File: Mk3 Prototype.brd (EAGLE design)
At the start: 113 x 55.2 mm, 193 parts, among them IC1 BD49XXX, IC2 NCP1529MU, IC3 STM32F401V, IC4 CC3100, IC5 S25FL216K0PMFI011, J1 ZX62-AB-5PA(11), J2 SFV30R-2STE1HLF, J3 SWD_SHROUD, Q1 DMMT5401, Q2 NTR4101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

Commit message: first prototype pretty much done
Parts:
- added ANT2: CHIPANT, TiLDA Mk3 Parts:2450AT42A100
- JP4: value M10SILK_FEMALE_PTH -> M10NOSILK; device SparkFun-Connectors:1X10 -> TiLDA Mk3 Parts:1X10-NOSILK
- SV1: device con-lstb:MA03-1 -> TiLDA Mk3 Parts:1X03
- moved LOGO1 28.3 mm to (75.4, 22.1), turned to 0 degrees
- moved C70 10.4 mm to (82.5, 53.0), turned to 180 degrees
- moved ANT1 4.92 mm to (75.0, 58.5), turned to 0 degrees
- moved C67 3.93 mm to (82.5, 50.0), turned to 180 degrees
- moved X6 3.08 mm to (86.0, 51.0)
- moved FID4 3.00 mm to (2.50, 3.00)
- moved L7 3.00 mm to (82.0, 51.6)
- moved R41 3.00 mm to (82.5, 51.0)
- moved SV1 2.50 mm to (90.5, 47.0)
- moved FID1 0.67 mm to (2.90, 46.3)
- moved FID6 0.67 mm to (2.90, 46.3)
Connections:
- net ANT: now also ANT2.P$1; no longer ANT1.FEED
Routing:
- net ANT: track 13.2 -> 3.27 mm
- net N$2: track 3.17 -> 6.17 mm
- net N$18: track 98.1 -> 97.3 mm
- net N$48: track 0.72 -> 1.42 mm
- net I2C_SCL: track 52.5 -> 53.1 mm
- net GND: track 210.9 -> 210.8 mm, vias 162 -> 154
- added copper zone on layer 1, net N$29
- added copper zone on layer 16, net N$29
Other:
- board text added: "*"
- board text added: "M. Brejza, LWK, parag0n"

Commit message: minor touchups
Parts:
- moved C67 0.50 mm to (83.0, 50.0)
- moved C70 0.50 mm to (83.0, 53.0)
- moved L7 0.50 mm to (82.5, 51.6)
- moved R41 0.50 mm to (83.0, 51.0)
- moved SV1 0.20 mm to (90.5, 46.8)
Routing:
- net GND: track 210.8 -> 216.6 mm, vias 154 -> 157
- net +3V3: track 516.0 -> 512.0 mm
- net N$19: track 8.06 -> 5.13 mm
- net ANT: track 3.27 -> 4.62 mm
- net N$17: track 31.8 -> 30.8 mm
- net CC_FLASH_CLK: track 18.4 -> 17.6 mm
- net N$48: track 1.42 -> 0.92 mm
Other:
- outline, holes or cut-outs redrawn

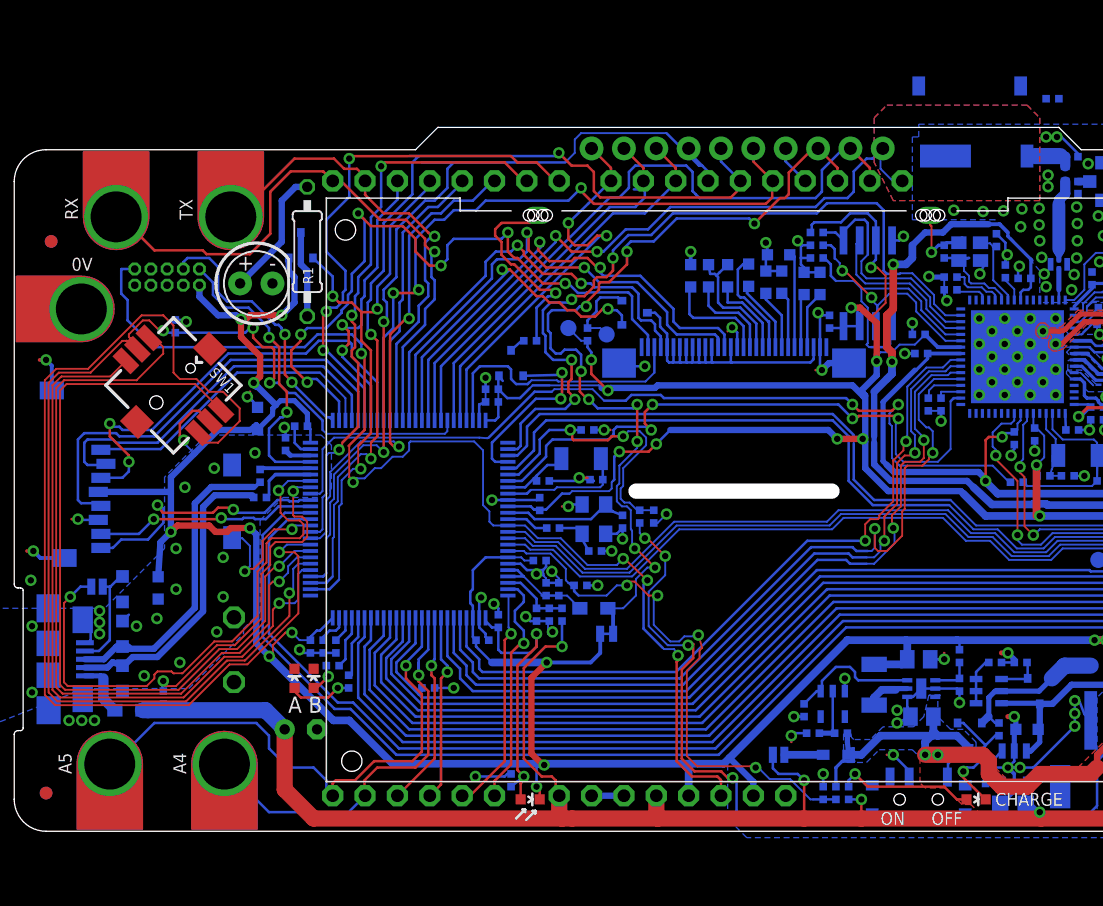
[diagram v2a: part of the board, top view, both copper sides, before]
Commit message: schematic tidyied up
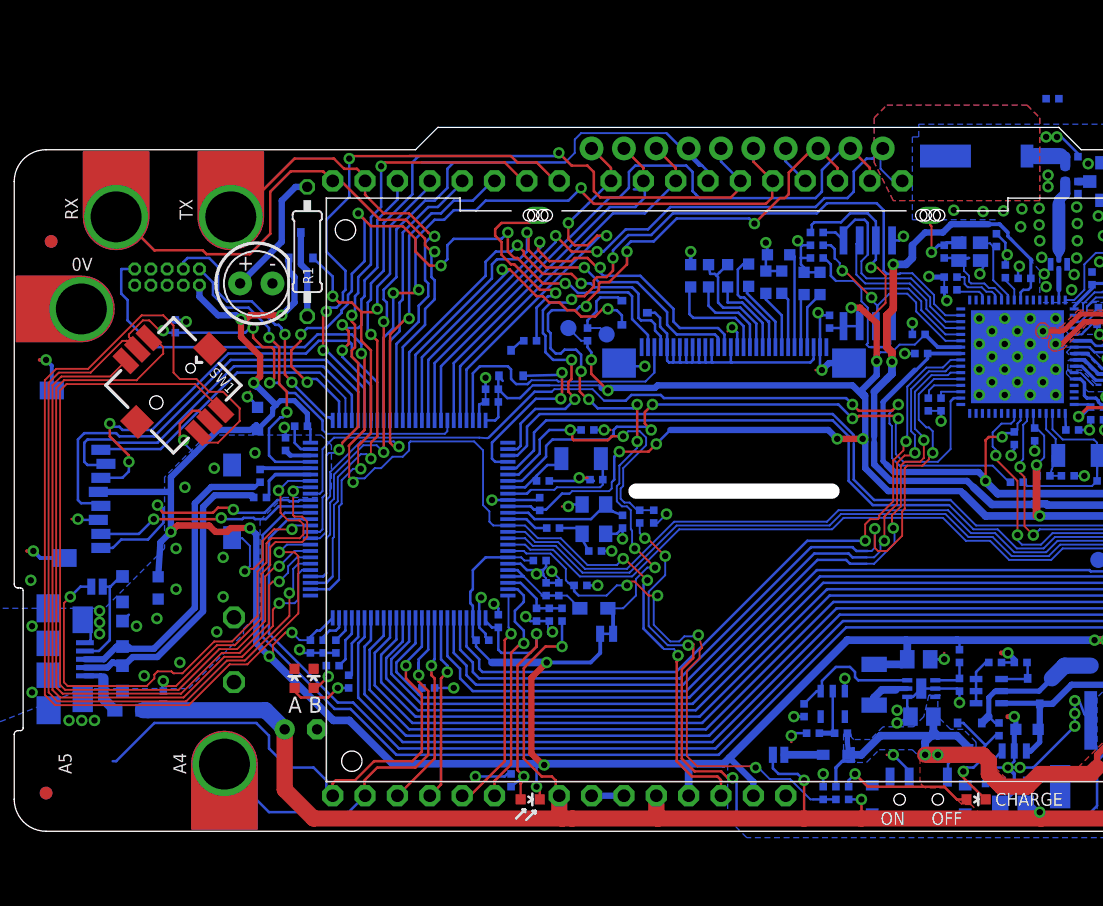
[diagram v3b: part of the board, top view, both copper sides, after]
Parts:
- removed ANT1: ANTENNA22500AT44M0400, SparkFun-RF:ANTENNA-CHIP_2500AT44M0400
- removed TP7: TP4MM, TiLDA Mk3 Parts:4MMEDGE
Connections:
- net A5: no longer TP7.P$1
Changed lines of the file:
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@@
 <?xml version="1.0" encoding="utf-8"?>
 <!DOCTYPE eagle SYSTEM "eagle.dtd">
-<eagle version="6.6.0">
+<eagle version="7.1.0">
 <drawing>
 <settings>
@@
 <pass name="Default">
 <param name="RoutingGrid" value="50mil"/>
+<param name="AutoGrid" value="1"/>
+<param name="Efforts" value="0"/>
+<param name="TopRouterVariant" value="1"/>
 <param name="tpViaShape" value="round"/>
 <param name="PrefDir.1" value="|"/>
@@
 <element name="TP8" library="TiLDA Mk3 Parts" package="4MMEDGE" value="TP4MM" x="16.5" y="4" smashed="yes" rot="R180"/>
 <element name="TP5" library="TiLDA Mk3 Parts" package="4MMEDGE" value="TP4MM" x="4" y="41" smashed="yes" rot="R90"/>
-<element name="TP7" library="TiLDA Mk3 Parts" package="4MMEDGE" value="TP4MM" x="7.5" y="4" smashed="yes" rot="R180"/>
 <element name="R18" library="TiLDA Mk3 Parts" package="R0402-SMALLER" value="0402/220k/5%" x="43" y="17" smashed="yes" rot="MR90">
 <attribute name="NAME" x="43.6015" y="15.889" size="0.8128" layer="26" font="vector" ratio="14" rot="MR270"/>
@@
 <attribute name="NAME" x="84.889" y="55.6985" size="0.8128" layer="26" font="vector" ratio="14" rot="MR0"/>
 </element>
-<element name="ANT1" library="SparkFun-RF" package="ANTENNA-CHIP_2500AT44M0400" value="ANTENNA22500AT44M0400" x="75" y="58.5" smashed="yes" rot="MR0"/>
 <element name="C8" library="TiLDA Mk3 Parts" package="C0402-SMALLER" value="0402/4u7/6.3V/X5R" x="37.5" y="34.7" smashed="yes" rot="MR180">
 <attribute name="NAME" x="36.389" y="34.5985" size="0.8128" layer="26" font="vector" ratio="14" rot="MR0"/>
@@
 <wire x1="30.75" y1="13.25" x2="32" y2="14.5" width="0.2" layer="16"/>
 <wire x1="32" y1="16.75" x2="32" y2="14.5" width="0.2" layer="16"/>
-<contactref element="TP7" pad="P$1"/>
 <wire x1="11" y1="8.5" x2="19" y2="8.5" width="0.2" layer="16"/>
 <wire x1="19" y1="8.5" x2="20" y2="7.5" width="0.2" layer="16"/>
@@
 <wire x1="11" y1="8.5" x2="8" y2="5.5" width="0.2" layer="16"/>
 <wire x1="8" y1="5.5" x2="7.73" y2="5.5" width="0.2" layer="16"/>
-<wire x1="7.73" y1="5.5" x2="7.5" y2="5.27" width="0.2" layer="16"/>
 </signal>
 <signal name="N$4">

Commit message: more tidying
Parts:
- added ANT1: ANTENNA22500AT44M0400, SparkFun-RF:ANTENNA-CHIP_2500AT44M0400
- added TP7: TP4MM, TiLDA Mk3 Parts:4MMEDGE
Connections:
- net A5: now also TP7.P$1
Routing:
- added copper zone on layer 1, net S$1
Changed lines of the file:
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@@
 <?xml version="1.0" encoding="utf-8"?>
 <!DOCTYPE eagle SYSTEM "eagle.dtd">
-<eagle version="7.1.0">
+<eagle version="6.6.0">
 <drawing>
 <settings>
@@
 <layer number="50" name="dxf" color="7" fill="1" visible="no" active="no"/>
 <layer number="51" name="tDocu" color="14" fill="1" visible="no" active="yes"/>
-<layer number="52" name="bDocu" color="3" fill="1" visible="no" active="yes"/>
+<layer number="52" name="bDocu" color="3" fill="1" visible="yes" active="yes"/>
 <layer number="53" name="tGND_GNDA" color="7" fill="9" visible="no" active="no"/>
 <layer number="54" name="bGND_GNDA" color="1" fill="9" visible="no" active="no"/>
@@
 <pass name="Default">
 <param name="RoutingGrid" value="50mil"/>
-<param name="AutoGrid" value="1"/>
-<param name="Efforts" value="0"/>
-<param name="TopRouterVariant" value="1"/>
 <param name="tpViaShape" value="round"/>
 <param name="PrefDir.1" value="|"/>
@@
 <element name="TP8" library="TiLDA Mk3 Parts" package="4MMEDGE" value="TP4MM" x="16.5" y="4" smashed="yes" rot="R180"/>
 <element name="TP5" library="TiLDA Mk3 Parts" package="4MMEDGE" value="TP4MM" x="4" y="41" smashed="yes" rot="R90"/>
+<element name="TP7" library="TiLDA Mk3 Parts" package="4MMEDGE" value="TP4MM" x="7.5" y="4" smashed="yes" rot="R180"/>
 <element name="R18" library="TiLDA Mk3 Parts" package="R0402-SMALLER" value="0402/220k/5%" x="43" y="17" smashed="yes" rot="MR90">
 <attribute name="NAME" x="43.6015" y="15.889" size="0.8128" layer="26" font="vector" ratio="14" rot="MR270"/>
@@
 <attribute name="NAME" x="84.889" y="55.6985" size="0.8128" layer="26" font="vector" ratio="14" rot="MR0"/>
 </element>
+<element name="ANT1" library="SparkFun-RF" package="ANTENNA-CHIP_2500AT44M0400" value="ANTENNA22500AT44M0400" x="75" y="58.5" smashed="yes" rot="MR0"/>
 <element name="C8" library="TiLDA Mk3 Parts" package="C0402-SMALLER" value="0402/4u7/6.3V/X5R" x="37.5" y="34.7" smashed="yes" rot="MR180">
 <attribute name="NAME" x="36.389" y="34.5985" size="0.8128" layer="26" font="vector" ratio="14" rot="MR0"/>
@@
 <wire x1="81" y1="54.5" x2="82.2" y2="54.5" width="0.2" layer="16"/>
 <wire x1="82.2" y1="54.5" x2="83.6" y2="53.1" width="0.2" layer="16"/>
-<wire x1="83.6" y1="53.1" x2="81" y2="57.5" width="0" layer="19" extent="1-16"/>
 <via x="81.15" y="50.6" extent="1-16" drill="0.5" shape="octagon"/>
 <via x="81.85" y="54.5" extent="1-16" drill="0.5" shape="octagon"/>
+<wire x1="81" y1="54.5" x2="81" y2="57.5" width="0" layer="19" extent="16-16"/>
 </signal>
 <signal name="LCD_POWER">
@@
 <wire x1="30.75" y1="13.25" x2="32" y2="14.5" width="0.2" layer="16"/>
 <wire x1="32" y1="16.75" x2="32" y2="14.5" width="0.2" layer="16"/>
+<contactref element="TP7" pad="P$1"/>
 <wire x1="11" y1="8.5" x2="19" y2="8.5" width="0.2" layer="16"/>
 <wire x1="19" y1="8.5" x2="20" y2="7.5" width="0.2" layer="16"/>
@@
 <wire x1="11" y1="8.5" x2="8" y2="5.5" width="0.2" layer="16"/>
 <wire x1="8" y1="5.5" x2="7.73" y2="5.5" width="0.2" layer="16"/>
+<wire x1="7.73" y1="5.5" x2="7.5" y2="5.27" width="0.2" layer="16"/>
 </signal>
 <signal name="N$4">
@@
 </polygon>
 </signal>
+<signal name="S$1">
+<polygon width="0.15" layer="1" pour="cutout">
+<vertex x="112.5" y="34.5"/>
+<vertex x="109.5" y="34.5"/>
+<vertex x="109.5" y="18"/>
+<vertex x="113" y="18"/>
+<vertex x="113" y="34.5"/>
+</polygon>
+</signal>

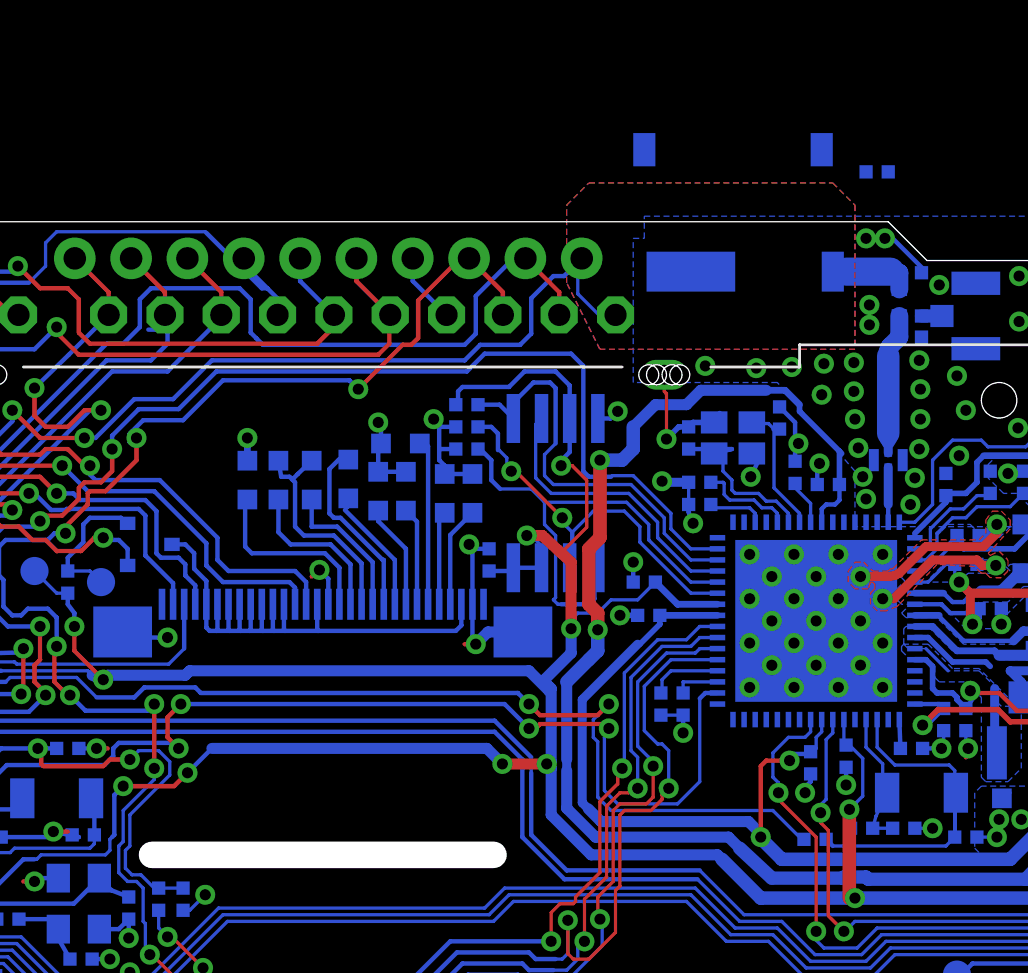
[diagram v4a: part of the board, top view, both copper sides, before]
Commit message: Removed errant R42 resisitor and old antenna footprint
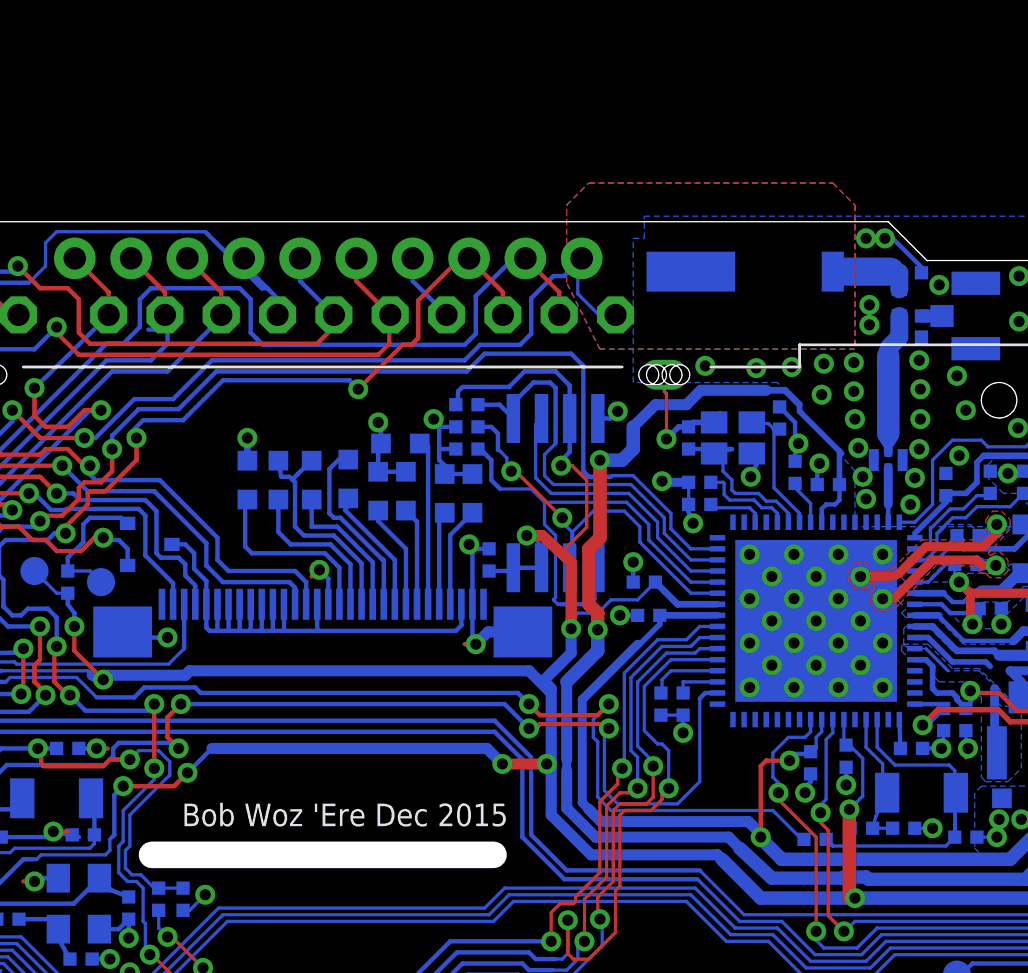
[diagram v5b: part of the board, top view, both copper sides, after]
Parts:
- removed ANT1: ANTENNA22500AT44M0400, SparkFun-RF:ANTENNA-CHIP_2500AT44M0400
- removed R42: 0402/100K/5%, TiLDA Mk3 Parts:R0402-SMALLER
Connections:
- net GND: no longer R42.2
- net WIFI_INTR: no longer R42.1
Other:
- board text added: "Bob Woz 'Ere Dec 2015"
- board text added: "M. Brejza, LWK, thinkl33t"
- board text removed: "M. Brejza, LWK, parag0n"
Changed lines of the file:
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@@
 <layer number="49" name="Reference" color="13" fill="1" visible="no" active="yes"/>
 <layer number="50" name="dxf" color="7" fill="1" visible="no" active="no"/>
-<layer number="51" name="tDocu" color="14" fill="1" visible="no" active="yes"/>
+<layer number="51" name="tDocu" color="14" fill="1" visible="yes" active="yes"/>
 <layer number="52" name="bDocu" color="3" fill="1" visible="yes" active="yes"/>
 <layer number="53" name="tGND_GNDA" color="7" fill="9" visible="no" active="no"/>
@@
 <wire x1="86.1" y1="31" x2="86.1" y2="28.8" width="0.15" layer="26"/>
 <wire x1="86.1" y1="28.8" x2="87.7" y2="27.2" width="0.15" layer="26"/>
-<text x="88.1" y="16.3" size="1.27" layer="22" font="vector" ratio="14" rot="MR0">M. Brejza, LWK, parag0n</text>
+<text x="88.1" y="16.3" size="1.27" layer="22" font="vector" ratio="14" rot="MR0">M. Brejza, LWK, thinkl33t</text>
 <wire x1="78.1" y1="9.2" x2="77.7" y2="9.2" width="0.15" layer="26"/>
 <wire x1="77.7" y1="9.2" x2="77.5" y2="9" width="0.15" layer="26"/>
@@
 <text x="62.1" y="44.6" size="0.8128" layer="26" font="vector" rot="MR0">*</text>
 <rectangle x1="75" y1="33.5" x2="82.5" y2="41" layer="29"/>
+<text x="57.5" y="28.5" size="1.016" layer="21" font="fixed" align="center">Bob Woz 'Ere Dec 2015 </text>
 </plain>
 <attributes>
@@
 <attribute name="NAME" x="72.0515" y="32.489" size="0.8128" layer="26" font="vector" ratio="14" rot="MR270"/>
 </element>
-<element name="R42" library="TiLDA Mk3 Parts" package="R0402-SMALLER" value="0402/100K/5%" x="81.5" y="57.5" smashed="yes" rot="MR0">
-<attribute name="NAME" x="82.389" y="58.1985" size="0.8128" layer="26" font="vector" ratio="14" rot="MR0"/>
-</element>
 <element name="J3" library="dtb" package="SWD_PTH_SHROUD" value="SWD_SHROUD" x="12" y="43.5" smashed="yes" rot="MR0"/>
 <element name="U4" library="TiLDA Mk3 Parts" package="MICRO-SD-SOCKET-PP" value="USD-SOCKETNEW" x="17.5" y="21" smashed="yes" rot="MR270">
@@
 <attribute name="NAME" x="84.889" y="55.6985" size="0.8128" layer="26" font="vector" ratio="14" rot="MR0"/>
 </element>
-<element name="ANT1" library="SparkFun-RF" package="ANTENNA-CHIP_2500AT44M0400" value="ANTENNA22500AT44M0400" x="75" y="58.5" smashed="yes" rot="MR0"/>
 <element name="C8" library="TiLDA Mk3 Parts" package="C0402-SMALLER" value="0402/4u7/6.3V/X5R" x="37.5" y="34.7" smashed="yes" rot="MR180">
 <attribute name="NAME" x="36.389" y="34.5985" size="0.8128" layer="26" font="vector" ratio="14" rot="MR0"/>
@@
 <contactref element="C64" pad="1"/>
 <contactref element="R28" pad="2"/>
-<contactref element="R42" pad="2"/>
 <contactref element="J3" pad="3"/>
 <contactref element="J3" pad="9"/>
@@
 <via x="81.15" y="50.6" extent="1-16" drill="0.5" shape="octagon"/>
 <via x="81.85" y="54.5" extent="1-16" drill="0.5" shape="octagon"/>
-<wire x1="81" y1="54.5" x2="81" y2="57.5" width="0" layer="19" extent="16-16"/>
 </signal>
 <signal name="LCD_POWER">
@@
 <signal name="WIFI_INTR">
 <contactref element="IC4" pad="15"/>
-<contactref element="R42" pad="1"/>
 <contactref element="IC3" pad="2"/>
 <wire x1="38.75" y1="30" x2="39.5" y2="30" width="0.2" layer="16"/>
@@
 <wire x1="41.7" y1="37.6" x2="42.3" y2="37" width="0.2" layer="16"/>
 <wire x1="42.3" y1="37" x2="43.75" y2="37" width="0.2" layer="16"/>
-<wire x1="68.25" y1="48.75" x2="82" y2="57.5" width="0" layer="19" extent="16-16"/>
 </signal>
 <signal name="WIFI_!HIB">

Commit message: tweeking values of crystal caps
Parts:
- C20, C21: value 0402/6.2p/50V/NP0 -> 0402/6.0p/50V/NP0
- C65, C68: value 0402/6p2/100V/NP0 -> 0402/6.0p/50V/NP0
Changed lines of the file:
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@@
 </element>
 <element name="X5" library="TiLDA Mk3 Parts" package="CRYSTAL-2.5X2.0" value="Q24FA20H00396" x="75" y="45.5" smashed="yes" rot="MR0"/>
-<element name="C65" library="TiLDA Mk3 Parts" package="C0402-SMALLER" value="0402/6p2/100V/NP0" x="73" y="45.5" smashed="yes" rot="MR270">
+<element name="C65" library="TiLDA Mk3 Parts" package="C0402-SMALLER" value="0402/6.0p/50V/NP0" x="73" y="45.5" smashed="yes" rot="MR270">
 <attribute name="NAME" x="71.6985" y="44.611" size="0.8128" layer="26" font="vector" ratio="14" rot="MR90"/>
 </element>
-<element name="C68" library="TiLDA Mk3 Parts" package="C0402-SMALLER" value="0402/6p2/100V/NP0" x="77.1" y="46.4" smashed="yes" rot="MR270">
+<element name="C68" library="TiLDA Mk3 Parts" package="C0402-SMALLER" value="0402/6.0p/50V/NP0" x="77.1" y="46.4" smashed="yes" rot="MR270">
 <attribute name="NAME" x="76.689" y="46.9985" size="0.8128" layer="26" font="vector" ratio="14" rot="MR0"/>
 </element>
@@
 <attribute name="NAME" x="43.8" y="26.35" size="0.8128" layer="26" font="vector" ratio="14" rot="MR270"/>
 </element>
-<element name="C21" library="TiLDA Mk3 Parts" package="C0402-SMALLER" value="0402/6.2p/50V/NP0" x="47.75" y="24.3" smashed="yes" rot="MR90">
+<element name="C21" library="TiLDA Mk3 Parts" package="C0402-SMALLER" value="0402/6.0p/50V/NP0" x="47.75" y="24.3" smashed="yes" rot="MR90">
 <attribute name="NAME" x="53.089" y="20.9485" size="0.8128" layer="26" font="vector" ratio="14" rot="MR0"/>
 </element>
-<element name="C20" library="TiLDA Mk3 Parts" package="C0402-SMALLER" value="0402/6.2p/50V/NP0" x="45.6" y="22" smashed="yes" rot="MR0">
+<element name="C20" library="TiLDA Mk3 Parts" package="C0402-SMALLER" value="0402/6.0p/50V/NP0" x="45.6" y="22" smashed="yes" rot="MR0">
 <attribute name="NAME" x="46.589" y="20.7985" size="0.8128" layer="26" font="vector" ratio="14" rot="MR0"/>
 </element>
